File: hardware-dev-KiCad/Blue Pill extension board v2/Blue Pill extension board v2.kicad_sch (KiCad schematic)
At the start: 12 parts, among them J1 NRF_MODULE, J2 Conn_02x20_Odd_Even, J3 SD_CARD, J4 Conn_02x20_Odd_Even, J5 GPS_MODULE, J6 HUM & TEMP SENSOR, U1 YAAJ_BluePill_Part_Like

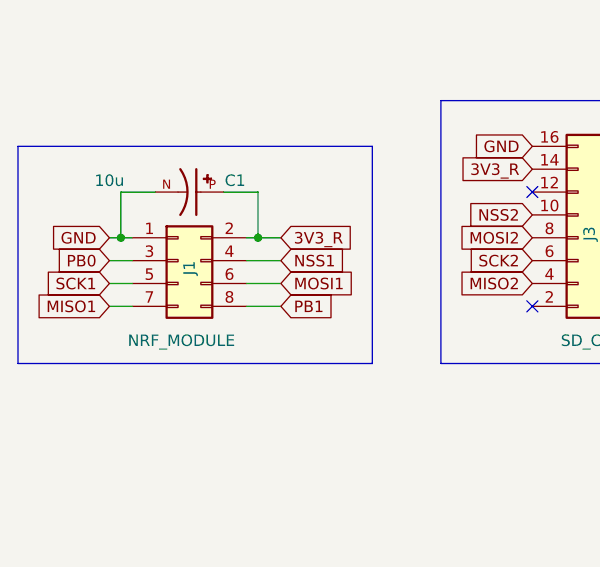
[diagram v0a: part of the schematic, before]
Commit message: Cambios de routeo y añado PCB para funcionar sin PTH
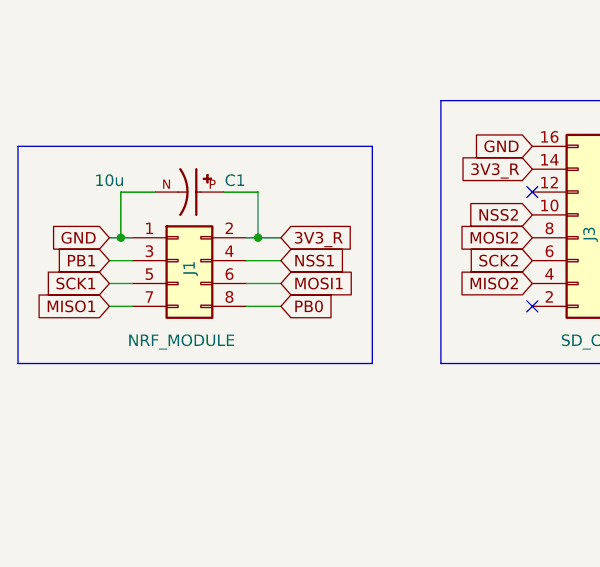
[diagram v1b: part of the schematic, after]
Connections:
- net PB0: now also J1.8 (Pin_8); no longer J1.3 (Pin_3)
- net PB1: now also J1.3 (Pin_3); no longer J1.8 (Pin_8)

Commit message: Modifico placa para hacerla de una sola capa
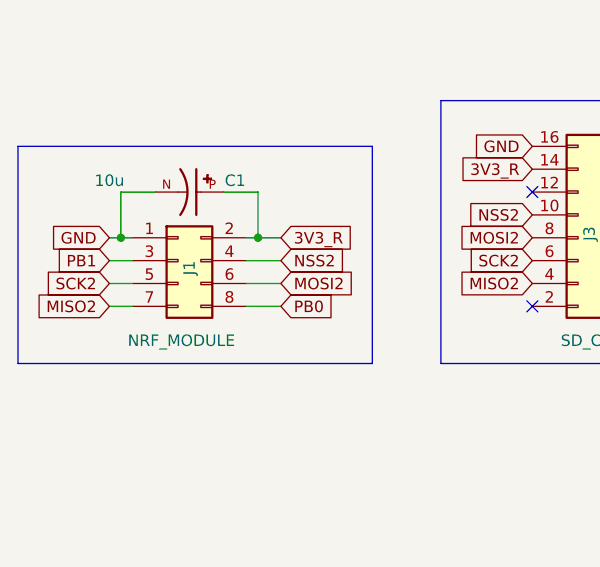
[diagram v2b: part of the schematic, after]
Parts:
- R1, R2, R3, R4: footprint Resistor_SMD:R_0805_2012Metric_Pad1.20x1.40mm_HandSolder -> Resistor_THT:R_Axial_DIN0207_L6.3mm_D2.5mm_P7.62mm_Horizontal
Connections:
- net MISO1: no longer J1.7 (Pin_7)
- net MISO2: now also J1.7 (Pin_7)
- net MOSI1: no longer J1.6 (Pin_6)
- net MOSI2: now also J1.6 (Pin_6)
- net NSS1: no longer J1.4 (Pin_4)
- net NSS2: now also J1.4 (Pin_4)
- net SCK1: no longer J1.5 (Pin_5)
- net SCK2: now also J1.5 (Pin_5)
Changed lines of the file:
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@@
 		)
 	)
-	(global_label "SCK1"
+	(global_label "SCK2"
 		(shape input)
 		(at 55.88 52.07 180)
@@
 		)
 	)
-	(global_label "MISO1"
+	(global_label "MISO2"
 		(shape input)
 		(at 55.88 54.61 180)
@@
 		)
 	)
-	(global_label "MOSI1"
+	(global_label "MOSI2"
 		(shape input)
 		(at 74.93 52.07 0)
@@
 		)
 	)
-	(global_label "NSS1"
+	(global_label "NSS2"
 		(shape input)
 		(at 74.93 49.53 0)
@@
 			)
 		)
-		(property "Footprint" "Resistor_SMD:R_0805_2012Metric_Pad1.20x1.40mm_HandSolder"
+		(property "Footprint" "Resistor_THT:R_Axial_DIN0207_L6.3mm_D2.5mm_P7.62mm_Horizontal"
 			(at 239.268 43.18 90)
 			(effects
@@
 			)
 		)
-		(property "Footprint" "Resistor_SMD:R_0805_2012Metric_Pad1.20x1.40mm_HandSolder"
+		(property "Footprint" "Resistor_THT:R_Axial_DIN0207_L6.3mm_D2.5mm_P7.62mm_Horizontal"
 			(at 211.582 43.18 90)
 			(effects
@@
 			)
 		)
-		(property "Footprint" "Resistor_SMD:R_0805_2012Metric_Pad1.20x1.40mm_HandSolder"
+		(property "Footprint" "Resistor_THT:R_Axial_DIN0207_L6.3mm_D2.5mm_P7.62mm_Horizontal"
 			(at 240.792 43.18 90)
 			(effects
@@
 			)
 		)
-		(property "Footprint" "Resistor_SMD:R_0805_2012Metric_Pad1.20x1.40mm_HandSolder"
+		(property "Footprint" "Resistor_THT:R_Axial_DIN0207_L6.3mm_D2.5mm_P7.62mm_Horizontal"
 			(at 206.502 43.18 90)
 			(effects
